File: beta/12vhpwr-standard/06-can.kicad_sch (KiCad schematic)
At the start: 6 parts, among them U2 TJA1051T/3

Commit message: Audit BETA electrical and pour pipeline
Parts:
- U2: MPN TJA1051T/3 -> TJA1051T/3/1J; Manufacturer NXP -> NXP Semiconductors
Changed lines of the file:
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@@
 		(property "Value" "TJA1051T/3" (at 156.21 67.31 0) (effects (font (size 1.27 1.27))))
 		(property "Footprint" "cec-Package_SO:SOIC-8_3.9x4.9mm_P1.27mm" (at 156.21 88.9 0) (effects (font (size 1.27 1.27)) (hide yes)))
-		(property "Datasheet" "" (at 156.21 88.9 0) (effects (font (size 1.27 1.27)) (hide yes)))
-		(property "Manufacturer" "NXP" (at 156.21 88.9 0) (effects (font (size 1.27 1.27)) (hide yes)))
-		(property "MPN" "TJA1051T/3" (at 156.21 88.9 0) (effects (font (size 1.27 1.27)) (hide yes)))
+		(property "Datasheet" "https://www.nxp.com/docs/en/data-sheet/TJA1051.pdf" (at 156.21 88.9 0) (effects (font (size 1.27 1.27)) (hide yes)))
+		(property "Manufacturer" "NXP Semiconductors" (at 156.21 88.9 0) (effects (font (size 1.27 1.27)) (hide yes)))
+		(property "MPN" "TJA1051T/3/1J" (at 156.21 88.9 0) (effects (font (size 1.27 1.27)) (hide yes)))
 		(property "LCSC" "C38695" (at 156.21 88.9 0) (effects (font (size 1.27 1.27)) (hide yes)))
 		(pin "1")

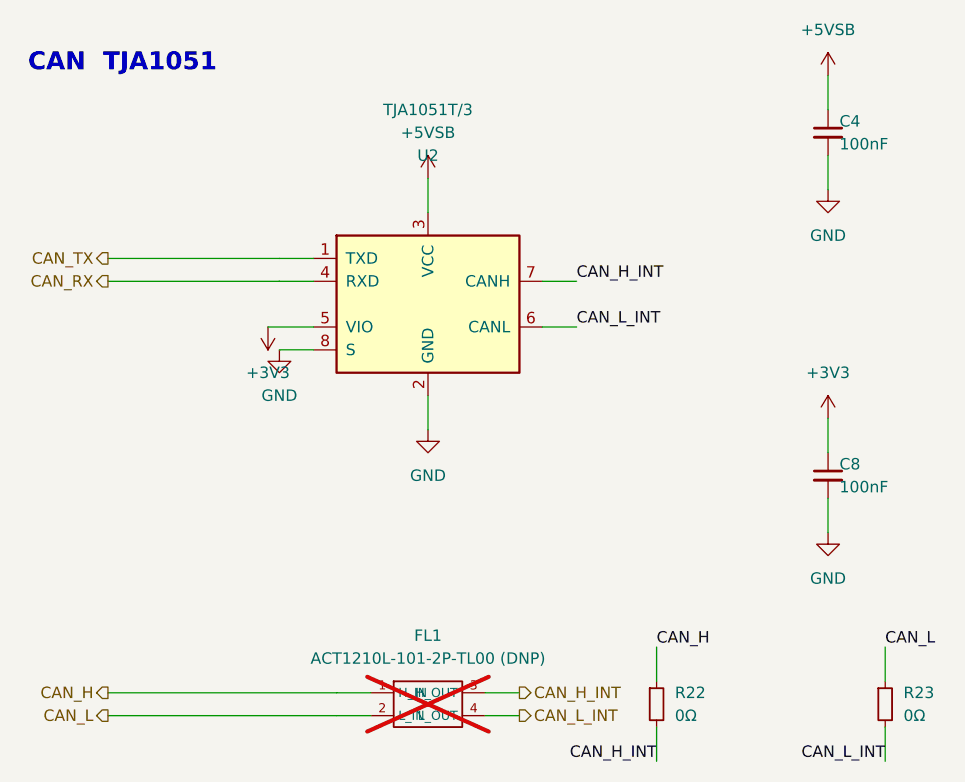
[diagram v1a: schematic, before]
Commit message: Audit BETA power designs and harden PCB pipeline
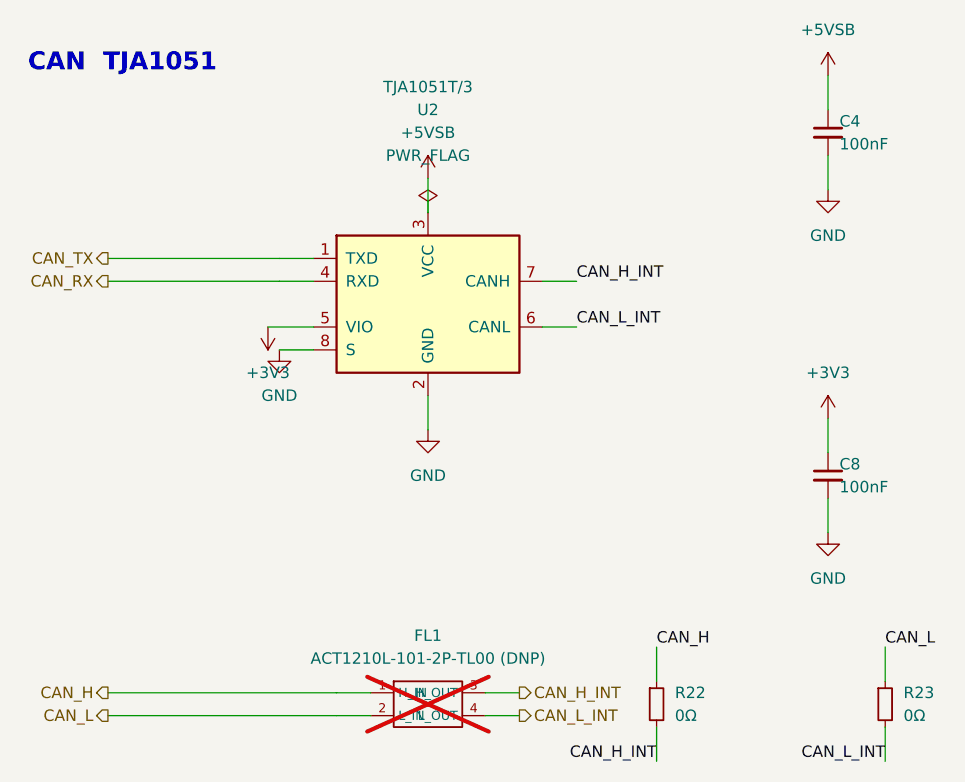
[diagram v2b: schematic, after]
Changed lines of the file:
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@@
 		(dnp no)
 		(fields_autoplaced yes)
-		(property "Reference" "U2" (at 156.21 72.39 0) (effects (font (size 1.27 1.27))))
-		(property "Value" "TJA1051T/3" (at 156.21 67.31 0) (effects (font (size 1.27 1.27))))
+		(property "Reference" "U2" (at 156.21 67.31 0) (effects (font (size 1.27 1.27))))
+		(property "Value" "TJA1051T/3" (at 156.21 64.77 0) (effects (font (size 1.27 1.27))))
 		(property "Footprint" "cec-Package_SO:SOIC-8_3.9x4.9mm_P1.27mm" (at 156.21 88.9 0) (effects (font (size 1.27 1.27)) (hide yes)))
 		(property "Datasheet" "https://www.nxp.com/docs/en/data-sheet/TJA1051.pdf" (at 156.21 88.9 0) (effects (font (size 1.27 1.27)) (hide yes)))
@@
 		(property "Value" "100nF" (at 201.93 71.12 0) (effects (font (size 1.27 1.27)) (justify left)))
 		(property "Footprint" "cec-Capacitor_SMD:C_0402_1005Metric" (at 200.66 69.85 0) (effects (font (size 1.27 1.27)) (hide yes)))
-		(property "Datasheet" "" (at 200.66 69.85 0) (effects (font (size 1.27 1.27)) (hide yes)))
+		(property "Datasheet" "https://product.samsungsem.com/mlcc/CL05B104KO5NNN.do" (at 200.66 69.85 0) (effects (font (size 1.27 1.27)) (hide yes)))
 		(property "Manufacturer" "Samsung" (at 200.66 69.85 0) (effects (font (size 1.27 1.27)) (hide yes)))
 		(property "MPN" "CL05B104KO5NNNC" (at 200.66 69.85 0) (effects (font (size 1.27 1.27)) (hide yes)))
@@
 		(property "Value" "100nF" (at 201.93 109.22 0) (effects (font (size 1.27 1.27)) (justify left)))
 		(property "Footprint" "cec-Capacitor_SMD:C_0402_1005Metric" (at 200.66 107.95 0) (effects (font (size 1.27 1.27)) (hide yes)))
-		(property "Datasheet" "" (at 200.66 107.95 0) (effects (font (size 1.27 1.27)) (hide yes)))
+		(property "Datasheet" "https://product.samsungsem.com/mlcc/CL05B104KO5NNN.do" (at 200.66 107.95 0) (effects (font (size 1.27 1.27)) (hide yes)))
 		(property "Manufacturer" "Samsung" (at 200.66 107.95 0) (effects (font (size 1.27 1.27)) (hide yes)))
 		(property "MPN" "CL05B104KO5NNNC" (at 200.66 107.95 0) (effects (font (size 1.27 1.27)) (hide yes)))
@@
 	)
 	(symbol
+		(lib_id "cec-power:PWR_FLAG")
+		(at 156.21 78.74 0)
+		(unit 1)
+		(exclude_from_sim no)
+		(in_bom yes)
+		(on_board yes)
+		(dnp no)
+		(property "Reference" "#PWR601" (at 156.21 76.2 0) (effects (font (size 1.27 1.27)) (hide yes)))
+		(property "Value" "PWR_FLAG" (at 156.21 72.39 0) (effects (font (size 1.27 1.27))))
+		(pin "1")
+		(instances
+			(project "12vhpwr-standard-module"
+				(path "/436b24cb-7227-4a56-93c7-4c5d9a5d0058/6f9d5a2e-6b0a-4b6b-9a7a-2f7a7a8a1a06" (reference "#PWR601") (unit 1))
+			)
+		)
+	)
+	(symbol
 		(lib_id "cec-power:GND")
 		(at 200.66 76.2 0)
@@
 		(on_board yes)
 		(dnp no)
-		(property "Reference" "#PWR601" (at 200.66 73.66 0) (effects (font (size 1.27 1.27)) (hide yes)))
+		(property "Reference" "#PWR602" (at 200.66 73.66 0) (effects (font (size 1.27 1.27)) (hide yes)))
 		(property "Value" "GND" (at 200.66 81.28 0) (effects (font (size 1.27 1.27))))
 		(pin "1")
 		(instances
 			(project "12vhpwr-standard-module"
-				(path "/436b24cb-7227-4a56-93c7-4c5d9a5d0058/6f9d5a2e-6b0a-4b6b-9a7a-2f7a7a8a1a06" (reference "#PWR601") (unit 1))
+				(path "/436b24cb-7227-4a56-93c7-4c5d9a5d0058/6f9d5a2e-6b0a-4b6b-9a7a-2f7a7a8a1a06" (reference "#PWR602") (unit 1))
 			)
 		)
@@
 		(on_board yes)
 		(dnp no)
-		(property "Reference" "#PWR602" (at 200.66 111.76 0) (effects (font (size 1.27 1.27)) (hide yes)))
+		(property "Reference" "#PWR603" (at 200.66 111.76 0) (effects (font (size 1.27 1.27)) (hide yes)))
 		(property "Value" "GND" (at 200.66 119.38 0) (effects (font (size 1.27 1.27))))
 		(pin "1")
 		(instances
 			(project "12vhpwr-standard-module"
-				(path "/436b24cb-7227-4a56-93c7-4c5d9a5d0058/6f9d5a2e-6b0a-4b6b-9a7a-2f7a7a8a1a06" (reference "#PWR602") (unit 1))
+				(path "/436b24cb-7227-4a56-93c7-4c5d9a5d0058/6f9d5a2e-6b0a-4b6b-9a7a-2f7a7a8a1a06" (reference "#PWR603") (unit 1))
 			)
 		)
@@
 		(on_board yes)
 		(dnp no)
-		(property "Reference" "#PWR603" (at 156.21 100.33 0) (effects (font (size 1.27 1.27)) (hide yes)))
+		(property "Reference" "#PWR604" (at 156.21 100.33 0) (effects (font (size 1.27 1.27)) (hide yes)))
 		(property "Value" "GND" (at 156.21 107.95 0) (effects (font (size 1.27 1.27))))
 		(pin "1")
 		(instances
 			(project "12vhpwr-standard-module"
-				(path "/436b24cb-7227-4a56-93c7-4c5d9a5d0058/6f9d5a2e-6b0a-4b6b-9a7a-2f7a7a8a1a06" (reference "#PWR603") (unit 1))
+				(path "/436b24cb-7227-4a56-93c7-4c5d9a5d0058/6f9d5a2e-6b0a-4b6b-9a7a-2f7a7a8a1a06" (reference "#PWR604") (unit 1))
 			)
 		)
@@
 		(on_board yes)
 		(dnp no)
-		(property "Reference" "#PWR604" (at 139.7 91.44 0) (effects (font (size 1.27 1.27)) (hide yes)))
+		(property "Reference" "#PWR605" (at 139.7 91.44 0) (effects (font (size 1.27 1.27)) (hide yes)))
 		(property "Value" "GND" (at 139.7 99.06 0) (effects (font (size 1.27 1.27))))
 		(pin "1")
 		(instances
 			(project "12vhpwr-standard-module"
-				(path "/436b24cb-7227-4a56-93c7-4c5d9a5d0058/6f9d5a2e-6b0a-4b6b-9a7a-2f7a7a8a1a06" (reference "#PWR604") (unit 1))
+				(path "/436b24cb-7227-4a56-93c7-4c5d9a5d0058/6f9d5a2e-6b0a-4b6b-9a7a-2f7a7a8a1a06" (reference "#PWR605") (unit 1))
 			)
 		)
@@
 		(on_board yes)
 		(dnp no)
-		(property "Reference" "#PWR605" (at 200.66 60.96 0) (effects (font (size 1.27 1.27)) (hide yes)))
+		(property "Reference" "#PWR606" (at 200.66 60.96 0) (effects (font (size 1.27 1.27)) (hide yes)))
 		(property "Value" "+5VSB" (at 200.66 58.42 0) (effects (font (size 1.27 1.27))))
 		(pin "1")
 		(instances
 			(project "12vhpwr-standard-module"
-				(path "/436b24cb-7227-4a56-93c7-4c5d9a5d0058/6f9d5a2e-6b0a-4b6b-9a7a-2f7a7a8a1a06" (reference "#PWR605") (unit 1))
+				(path "/436b24cb-7227-4a56-93c7-4c5d9a5d0058/6f9d5a2e-6b0a-4b6b-9a7a-2f7a7a8a1a06" (reference "#PWR606") (unit 1))
 			)
 		)
@@
 		(on_board yes)
 		(dnp no)
-		(property "Reference" "#PWR606" (at 156.21 72.39 0) (effects (font (size 1.27 1.27)) (hide yes)))
+		(property "Reference" "#PWR607" (at 156.21 72.39 0) (effects (font (size 1.27 1.27)) (hide yes)))
 		(property "Value" "+5VSB" (at 156.21 69.85 0) (effects (font (size 1.27 1.27))))
 		(pin "1")
 		(instances
 			(project "12vhpwr-standard-module"
-				(path "/436b24cb-7227-4a56-93c7-4c5d9a5d0058/6f9d5a2e-6b0a-4b6b-9a7a-2f7a7a8a1a06" (reference "#PWR606") (unit 1))
+				(path "/436b24cb-7227-4a56-93c7-4c5d9a5d0058/6f9d5a2e-6b0a-4b6b-9a7a-2f7a7a8a1a06" (reference "#PWR607") (unit 1))
 			)
 		)
@@
 		(on_board yes)
 		(dnp no)
-		(property "Reference" "#PWR607" (at 200.66 99.06 0) (effects (font (size 1.27 1.27)) (hide yes)))
+		(property "Reference" "#PWR608" (at 200.66 99.06 0) (effects (font (size 1.27 1.27)) (hide yes)))
 		(property "Value" "+3V3" (at 200.66 96.52 0) (effects (font (size 1.27 1.27))))
 		(pin "1")
 		(instances
 			(project "12vhpwr-standard-module"
-				(path "/436b24cb-7227-4a56-93c7-4c5d9a5d0058/6f9d5a2e-6b0a-4b6b-9a7a-2f7a7a8a1a06" (reference "#PWR607") (unit 1))
+				(path "/436b24cb-7227-4a56-93c7-4c5d9a5d0058/6f9d5a2e-6b0a-4b6b-9a7a-2f7a7a8a1a06" (reference "#PWR608") (unit 1))
 			)
 		)
@@
 		(on_board yes)
 		(dnp no)
-		(property "Reference" "#PWR608" (at 138.43 88.9 0) (effects (font (size 1.27 1.27)) (hide yes)))
+		(property "Reference" "#PWR609" (at 138.43 88.9 0) (effects (font (size 1.27 1.27)) (hide yes)))
 		(property "Value" "+3V3" (at 138.43 96.52 0) (effects (font (size 1.27 1.27))))
 		(pin "1")
 		(instances
 			(project "12vhpwr-standard-module"
-				(path "/436b24cb-7227-4a56-93c7-4c5d9a5d0058/6f9d5a2e-6b0a-4b6b-9a7a-2f7a7a8a1a06" (reference "#PWR608") (unit 1))
-			)
-		)
+				(path "/436b24cb-7227-4a56-93c7-4c5d9a5d0058/6f9d5a2e-6b0a-4b6b-9a7a-2f7a7a8a1a06" (reference "#PWR609") (unit 1))
+			)
+		)

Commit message: Rework BETA power rails and schematic composition
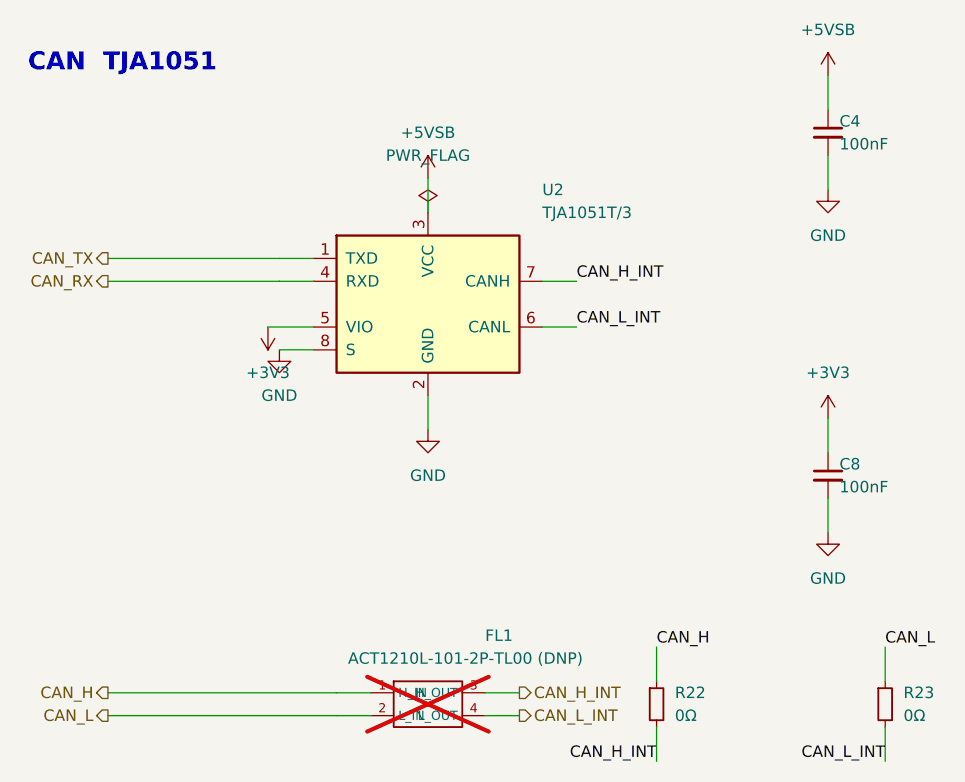
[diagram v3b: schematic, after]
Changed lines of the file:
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@@
 		(dnp no)
 		(fields_autoplaced yes)
-		(property "Reference" "U2" (at 156.21 67.31 0) (effects (font (size 1.27 1.27))))
-		(property "Value" "TJA1051T/3" (at 156.21 64.77 0) (effects (font (size 1.27 1.27))))
+		(property "Reference" "U2" (at 168.91 76.2 0) (effects (font (size 1.27 1.27)) (justify left)))
+		(property "Value" "TJA1051T/3" (at 168.91 78.74 0) (effects (font (size 1.27 1.27)) (justify left)))
 		(property "Footprint" "cec-Package_SO:SOIC-8_3.9x4.9mm_P1.27mm" (at 156.21 88.9 0) (effects (font (size 1.27 1.27)) (hide yes)))
 		(property "Datasheet" "https://www.nxp.com/docs/en/data-sheet/TJA1051.pdf" (at 156.21 88.9 0) (effects (font (size 1.27 1.27)) (hide yes)))
@@
 		(dnp yes)
 		(fields_autoplaced yes)
-		(property "Reference" "FL1" (at 156.21 125.73 0) (effects (font (size 1.27 1.27))))
-		(property "Value" "ACT1210L-101-2P-TL00 (DNP)" (at 156.21 128.27 0) (effects (font (size 1.27 1.27))))
+		(property "Reference" "FL1" (at 162.56 125.73 0) (effects (font (size 1.27 1.27)) (justify left)))
+		(property "Value" "ACT1210L-101-2P-TL00 (DNP)" (at 147.32 128.27 0) (effects (font (size 1.27 1.27)) (justify left)))
 		(property "Footprint" "" (at 156.21 133.35 0) (effects (font (size 1.27 1.27)) (hide yes)))
 		(property "Datasheet" "" (at 156.21 133.35 0) (effects (font (size 1.27 1.27)) (hide yes)))
